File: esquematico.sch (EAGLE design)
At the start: 1 part, among them U1 ROB-14450

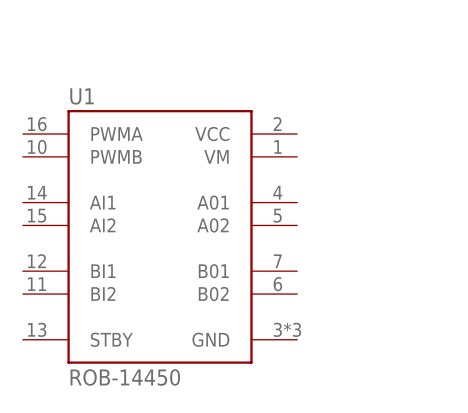
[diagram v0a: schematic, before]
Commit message: adicionei um led
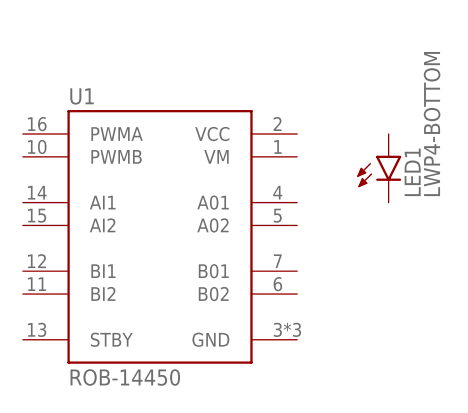
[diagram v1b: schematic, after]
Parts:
- added LED1: LWP4-BOTTOM, led:LWP4-BOTTOM
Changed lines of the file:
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@@
 <drawing>
 <settings>
-<setting alwaysvectorfont="yes"/>
+<setting alwaysvectorfont="no"/>
 <setting verticaltext="up"/>
 </settings>
@@
 <parts>
 <part name="U1" library="ROB-14450" deviceset="ROB-14450" device=""/>
+<part name="LED1" library="led" library_urn="urn:adsk.eagle:library:259" deviceset="*P4" device="-BOTTOM" package3d_urn="urn:adsk.eagle:package:15878/1" technology="LW"/>
 </parts>
 <sheets>
@@
 <attribute name="VALUE" x="-561.34" y="581.66" size="1.778" layer="96"/>
 </instance>
+<instance part="LED1" gate="G$1" x="-525.78" y="607.06" smashed="yes">
+<attribute name="NAME" x="-522.224" y="602.488" size="1.778" layer="95" rot="R90"/>
+<attribute name="VALUE" x="-520.065" y="602.488" size="1.778" layer="96" rot="R90"/>
+</instance>
 </instances>
 <busses>
@@
 </schematic>
 </drawing>
+<compatibility>
+<note version="8.2" severity="warning">
+Since Version 8.2, EAGLE supports online libraries. The ids
+of those online libraries will not be understood (or retained)
+with this version.
+</note>
+<note version="8.3" severity="warning">
+Since Version 8.3, EAGLE supports URNs for individual library
+assets (packages, symbols, and devices). The URNs of those assets
+will not be understood (or retained) with this version.
+</note>
+<note version="8.3" severity="warning">
+Since Version 8.3, EAGLE supports the association of 3D packages
+with devices in libraries, schematics, and board files. Those 3D
+packages will not be understood (or retained) with this version.
+</note>
+</compatibility>
 </eagle>
